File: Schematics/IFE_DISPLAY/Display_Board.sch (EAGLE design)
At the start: 48 parts, among them IC1 EP2C5T144, Q1 16MHz, U1 EPCS1SI8N, U2 MX150_8_PIN, U3 ATMEGA328P-AU, U4 HEX_CONVERTER, U5 HEX_CONVERTER, U6 MC7805BDD, U7 MCP1826S-1802E/DB, X3 16MHz

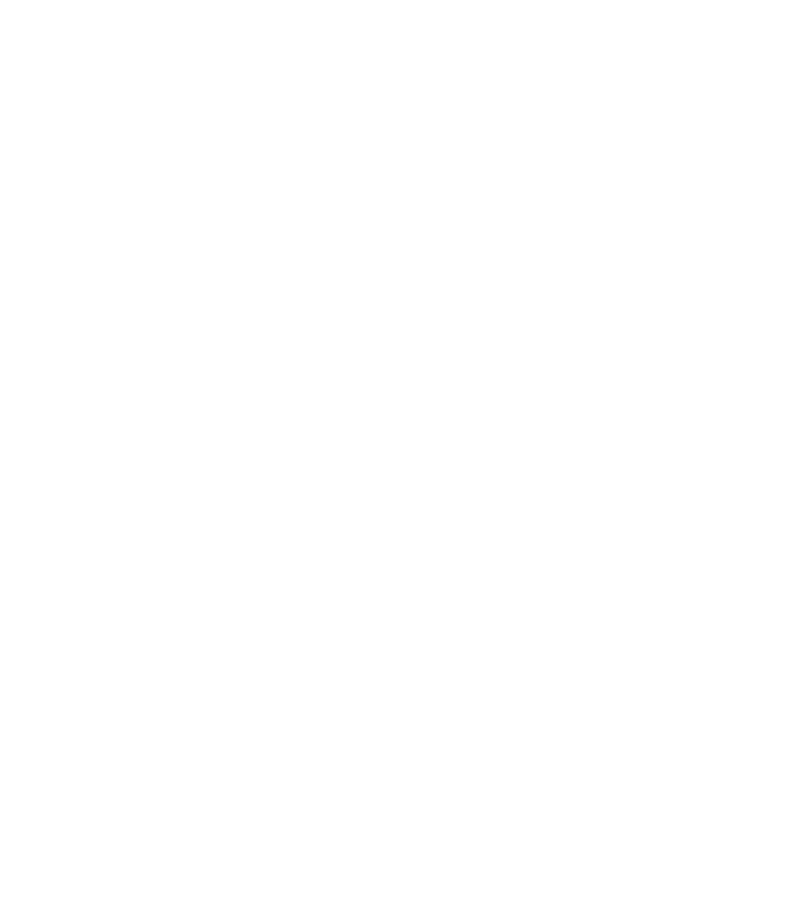
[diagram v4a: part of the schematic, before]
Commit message: Working on Breakout Board Layout
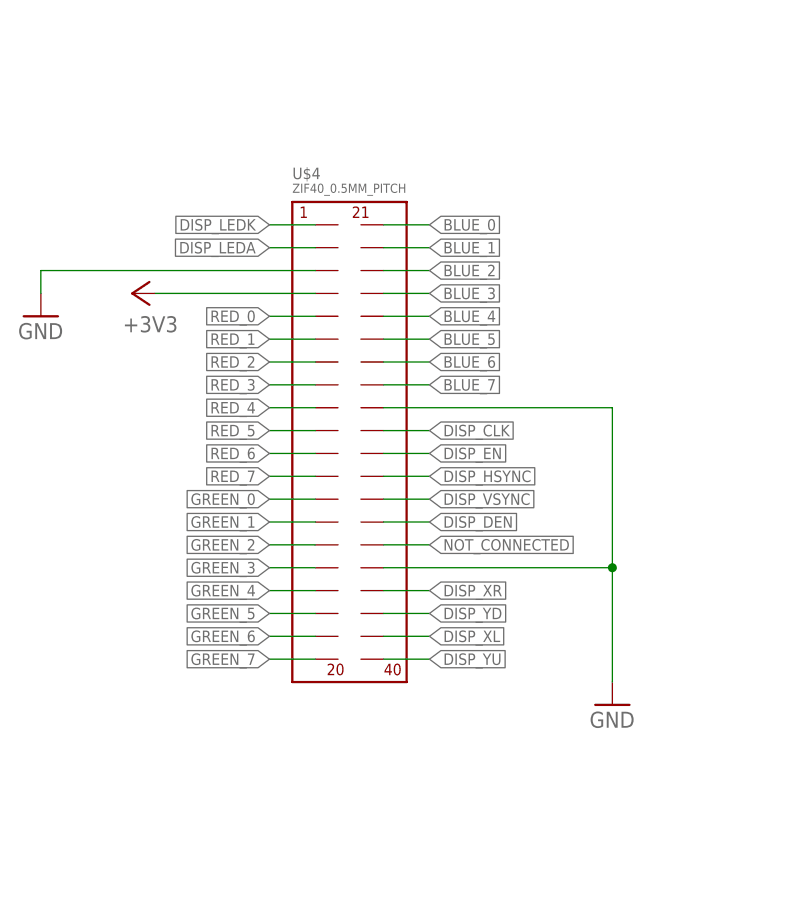
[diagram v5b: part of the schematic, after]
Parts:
- added U$4: ZIF40_0.5MM_PITCH, Connectors:ZIF40_0.5MM_PITCH
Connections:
- new net DISP_CLK: U$4.P$30
- new net DISP_DEN: U$4.P$34
- new net DISP_EN: U$4.P$31
- new net DISP_HSYNC: U$4.P$32
- new net DISP_LEDA: U$4.P$2
- new net DISP_LEDK: U$4.P$1
- new net DISP_VSYNC: U$4.P$33
- new net DISP_XL: U$4.P$39
- new net DISP_XR: U$4.P$37
- new net DISP_YD: U$4.P$38
- new net DISP_YU: U$4.P$40
- new net GREEN_3: U$4.P$16
- new net NOT_CONNECTED: U$4.P$35
- net +3V3: now also U$4.P$4
- net BLUE_0: now also U$4.P$21
- net BLUE_1: now also U$4.P$22
- net BLUE_2: now also U$4.P$23
- net BLUE_3: now also U$4.P$24
- net BLUE_4: now also U$4.P$25
- net BLUE_5: now also U$4.P$26
- net BLUE_6: now also U$4.P$27
- net BLUE_7: now also U$4.P$28
- net GND: now also U$4.P$29, U$4.P$3, U$4.P$36
- net GREEN_0: now also U$4.P$13
- net GREEN_1: now also U$4.P$14
- net GREEN_2: now also U$4.P$15
- net GREEN_4: now also U$4.P$17
- net GREEN_5: now also U$4.P$18
- net GREEN_6: now also U$4.P$19
- net GREEN_7: now also U$4.P$20
- net RED_0: now also U$4.P$5
- net RED_1: now also U$4.P$6
- net RED_2: now also U$4.P$7
- net RED_3: now also U$4.P$8
- net RED_4: now also U$4.P$9
- net RED_5: now also U$4.P$10
- net RED_6: now also U$4.P$11
- net RED_7: now also U$4.P$12

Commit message: figuring out DC-DC converters
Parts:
- removed C10: 0.1u, rcl:C-EUC0805K
- removed U$1: LM3940, Texas Instruments_By_element14_Batch_1:LM3940
- added D2: (no value), adafruit:DIODESMA
- added FUSE1: MINI297-3568, Fuse:MINI297-3568
- added R11, R16: 10k, rcl:R-US_R0805
- added U8: TPS5420D, Texas Instruments_By_element14_Batch_1:TPS5420D
- C1: value 0.1u -> 4.7uF; device rcl:C-EUC0805K -> resistor:C-EUC0805K
- C2: value 0.22u -> 0.01uF; device rcl:C-EUC0805K -> resistor:C-EUC0805K
- U6: value MC7805BDD -> TPS5420D; device IC's:MC7805BDD -> Texas Instruments_By_element14_Batch_1:TPS5420D
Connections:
- new net N$10: C2.2, U6.PH
- new net N$11: U6.VSENSE
- new net N$12: R11.1, R16.2, U6.ENA
- new net N$8: FUSE1.1, L2.1
- new net N$9: C2.1, U6.BOOT
- net +12V: now also C1.1, R11.2, U6.VIN; no longer C2.1, U6.IN
- net +3V3: no longer C10.1, U$1.VO, U7.VIN
- net +5V: no longer C1.1, U$1.VI, U6.OUT
- net GND: now also R16.1; no longer C10.2, C2.2, U$1.GND
- net PWR_IN: now also FUSE1.2; no longer L2.1
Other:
- moved on the sheet: C1, C11, C2, C5, L2, U7

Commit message: DCDC added need to adjust values
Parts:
- removed WIFI_: (no value), Headers_IFE:PINHD-2X4
- added C10, C12, C18, C19: 47uF, rcl:C-EUC0805K
- added C13, C20: 1800pF, rcl:C-EUC0805K
- added C14, C21: 0.1uF, rcl:C-EUC0805K
- added C15, C22: 150pF, rcl:C-EUC0805K
- added C16: 4.7uF, resistor:C-EUC0805K
- added C17: 0.01uF, resistor:C-EUC0805K
- added C23: 220u, Capacitors:C1206
- added D3: (no value), adafruit:DIODESMA
- added FUSE2: MINI297-3568, Fuse:MINI297-3568
- added L1: 23uH, Inductors:MSS7348
- added L3: 58uH, Inductors:MSS7348
- added L4: 20uH, Inductors:MSS7348
- added R17, R20, R21, R22: 10k, rcl:R-US_R0805
- added R18, R23: 5.9k, rcl:R-US_R0805
- added R19, R24: 549, rcl:R-US_R0805
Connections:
- net PWR_IN renamed PWR_IN_12
- new net +24V: C23.1, L4.2
- new net DISP_PWM: U3.PB1
- new net N$14: C14.2, R19.2
- new net N$15: C13.2, C14.1, C15.1, R17.1, R18.2, U6.VSENSE
- new net N$16: C17.1, U8.BOOT
- new net N$17: C17.2, D3.C, L3.1, U8.PH
- new net N$18: R20.1, R21.2, U8.ENA
- new net N$19: C20.2, C21.1, C22.1, R22.1, R23.2, U8.VSENSE
- new net N$20: C21.2, R24.2
- new net PWR_IN_24: FUSE2.2
- net +12V: now also C16.1, R20.2, U8.VIN
- net +3V3: now also C10.1, C12.1, C13.1, L1.2, R17.2, U7.VIN; no longer WIFI_.3, WIFI_.5, WIFI_.7
- net +5V: now also C18.1, C19.1, C20.1, L3.2, R22.2
- net GND: now also C10.2, C12.2, C15.2, C16.2, C18.2, C19.2, C22.2, C23.2, D2.A, D3.A, R18.1, R19.1, R21.1, R23.1, R24.1, U8.GND; no longer WIFI_.2
- net LED1: now also IC1.IO129
- net LED2: now also IC1.IO132
- net N$10: now also D2.C, L1.1
- net N$11: now also FUSE2.1, L4.1; no longer U6.VSENSE
- net RXD: no longer WIFI_.1
- net TXD_3_3: no longer WIFI_.8
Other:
- moved on the sheet: C1, C11, C2, C5, D2, FUSE1, L2, R11, R16, U6, U7, U8

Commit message: Finalizing Display Schematic
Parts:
- removed AS, JTAG: (no value), pinhead:PINHD-2X5
- removed C1, C16: 4.7uF, resistor:C-EUC0805K
- removed C10, C12, C18, C19: 47uF, rcl:C-EUC0805K
- removed C11: 0.1u, rcl:C-EUC0805K
- removed C13, C20: 1800pF, rcl:C-EUC0805K
- removed C14, C21: 0.1uF, rcl:C-EUC0805K
- removed C15, C22: 150pF, rcl:C-EUC0805K
- removed C17, C2: 0.01uF, resistor:C-EUC0805K
- removed C23, C5: 220u, Capacitors:C1206
- removed D2, D3: (no value), adafruit:DIODESMA
- removed FUSE1, FUSE2: MINI297-3568, Fuse:MINI297-3568
- removed IC1: EP2C5T144, altera-cyclone-II:EP2C5T144
- removed L1: 23uH, Inductors:MSS7348
- removed L2, L4: 20uH, Inductors:MSS7348
- removed L3: 58uH, Inductors:MSS7348
- removed QG1: SM77H, crystal:SM77H
- removed R1, R15, R2: 1K, resistor:R-US_R0805
- removed R11, R16, R17, R20, R21, R22: 10k, rcl:R-US_R0805
- removed R14: 10K, resistor:R-US_R0805
- removed R18, R23: 5.9k, rcl:R-US_R0805
- removed R19, R24: 549, rcl:R-US_R0805
- removed U6, U8: TPS5420D, Texas Instruments_By_element14_Batch_1:TPS5420D
- removed U7: MCP1826S-1802E/DB, Microchip_By_element14_Batch_1:MCP1826S-1802E/DB
- added AS1, JTAG1: (no value), pinhead:PINHD-2X5
- added C24, C40: 220u, Capacitors:C1206
- added C25: 0.1u, rcl:C-EUC0805K
- added C26, C33: 4.7uF, resistor:C-EUC0805K
- added C27, C34: 0.01uF, resistor:C-EUC0805K
- added C28, C29, C35, C36: 47uF, rcl:C-EUC0805K
- added C30, C37: 1800pF, rcl:C-EUC0805K
- added C31, C38: 0.1uF, rcl:C-EUC0805K
- added C32, C39: 150pF, rcl:C-EUC0805K
- added D4, D5: (no value), adafruit:DIODESMA
- added FUSE3, FUSE4: MINI297-3568, Fuse:MINI297-3568
- added IC2: EP2C5T144, altera-cyclone-II:EP2C5T144
- added L5, L8: 20uH, Inductors:MSS7348
- added L6: 23uH, Inductors:MSS7348
- added L7: 58uH, Inductors:MSS7348
- added Q2: MMBT3904L, transistor-npn:BCW31SMD
- added QG2: SM77H, crystal:SM77H
- added R25: 76, resistor:R-US_R0805
- added R26: 5.2k, resistor:R-US_R0805
- added R27, R28, R33: 1K, resistor:R-US_R0805
- added R29, R30, R31, R32: 10K, resistor:R-US_R0805
- added R34: 10k, rcl:R-US_R0805
- added R35: 5.9k, rcl:R-US_R0805
- added R36: 549, rcl:R-US_R0805
- added U$1: 776280-1, IFE_AMPSEAL_Conn:776280-1
- added U10, U9: TPS5420D, Texas Instruments_By_element14_Batch_1:TPS5420D
- R12: value 10K -> 5.9k; device resistor:R-US_R0805 -> rcl:R-US_R0805
- R13: value 10K -> 549; device resistor:R-US_R0805 -> rcl:R-US_R0805
- R3: value 10K -> 10k; device resistor:R-US_R0805 -> rcl:R-US_R0805
- U1: value EPCS1SI8N -> MCP1826S-1802E/DB; device Altera_By_element14_Batch_1:EPCS1SI8N -> Microchip_By_element14_Batch_1:MCP1826S-1802E/DB
- U2: value MX150_8_PIN -> EPCS1SI8N; device Connectors:MX150_8_PIN -> Altera_By_element14_Batch_1:EPCS1SI8N
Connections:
- removed net N$10: C2.2, D2.C, L1.1, U6.PH
- removed net N$11: FUSE2.1, L4.1
- removed net N$12: R11.1, R16.2, U6.ENA
- removed net N$14: C14.2, R19.2
- removed net N$15: C13.2, C14.1, C15.1, R17.1, R18.2, U6.VSENSE
- removed net N$16: C17.1, U8.BOOT
- removed net N$17: C17.2, D3.C, L3.1, U8.PH
- removed net N$18: R20.1, R21.2, U8.ENA
- removed net N$19: C20.2, C21.1, C22.1, R22.1, R23.2, U8.VSENSE
- removed net N$20: C21.2, R24.2
- removed net N$8: FUSE1.1, L2.1
- removed net N$9: C2.1, U6.BOOT
- removed net TXD_3_3: U5.6Y
- new net N$13: Q2.B, R26.1
- new net N$21: IC2.NSTATUS, R29.1
- new net N$22: C27.1, U9.BOOT
- new net N$23: C27.2, D4.C, L6.1, U9.PH
- new net N$25: C30.2, C31.1, C32.1, R12.2, R3.1, U9.VSENSE
- new net N$26: C31.2, R13.2
- new net N$27: C34.1, U10.BOOT
- new net N$28: C34.2, D5.C, L7.1, U10.PH
- new net N$30: C37.2, C38.1, C39.1, R34.1, R35.2, U10.VSENSE
- new net N$31: C38.2, R36.2
- new net N$32: FUSE4.1, L8.1
- net +12V: now also C24.1, C26.1, C33.1, L5.2, U10.ENA, U10.VIN, U9.ENA, U9.VIN; no longer C1.1, C16.1, C5.1, L2.2, R11.2, R20.2, U6.VIN, U8.VIN
- net +24V: now also C40.1, L8.2, R25.2; no longer C23.1, L4.2
- net +3V3: now also AS1.4, C28.1, C29.1, C30.1, IC2.VCC@1, IC2.VCC@10, IC2.VCC@11, IC2.VCC@12, IC2.VCC@13, IC2.VCC@16, IC2.VCC@18, IC2.VCC@2, IC2.VCC@20, IC2.VCC@3, IC2.VCC@6, IC2.VCC@8, JTAG1.4, L6.2, QG2.VCC, R28.1, R29.2, R31.2, R32.2, R33.2, U1.VIN, U2.VCC, U2.VCC_2, U2.VCC_3; no longer AS.4, C10.1, C12.1, C13.1, IC1.VCC@1, IC1.VCC@10, IC1.VCC@11, IC1.VCC@12, IC1.VCC@13, IC1.VCC@16, IC1.VCC@18, IC1.VCC@2, IC1.VCC@20, IC1.VCC@3, IC1.VCC@6, IC1.VCC@8, JTAG.4, L1.2, QG1.VCC, R13.2, R14.2, R15.2, R17.2, R2.1, R7.2, U1.VCC, U1.VCC_2, U1.VCC_3, U3.AVCC, U3.VCC, U3.VCC_2, U7.VIN
- net +5V: now also C35.1, C36.1, C37.1, L7.2, R34.2, R7.2, U3.AVCC, U3.VCC, U3.VCC_2; no longer C18.1, C19.1, C20.1, L3.2, R22.2
- net 50_MHZ: now also IC2.CLK0, QG2.OUT; no longer IC1.CLK0, QG1.OUT
- net ASDO: now also AS1.9, IC2.IO1, U2.ASDI; no longer AS.9, IC1.IO1, U1.ASDI
- net BLUE_0: now also IC2.IO52; no longer IC1.IO52
- net BLUE_1: now also IC2.IO53; no longer IC1.IO53
- net BLUE_2: now also IC2.IO55; no longer IC1.IO55
- net BLUE_3: now also IC2.IO57; no longer IC1.IO57
- net BLUE_4: now also IC2.IO58; no longer IC1.IO58
- net BLUE_5: now also IC2.IO59; no longer IC1.IO59
- net BLUE_6: now also IC2.IO60; no longer IC1.IO60
- net BLUE_7: now also IC2.IO63; no longer IC1.IO63
- net CANH: now also U$1.5; no longer U2.2
- net CANL: now also U$1.8; no longer U2.1
- net CONF_DONE: now also AS1.3, IC2.CONF_DONE, R32.1; no longer AS.3, IC1.CONF_DONE, R14.1
- net DATA0: now also AS1.7, IC2.DATA0, U2.DATA; no longer AS.7, IC1.DATA0, U1.DATA
- net DCLK: now also AS1.1, IC2.DCLK, U2.DCLK; no longer AS.1, IC1.DCLK, U1.DCLK
- net DISP_CLK: now also IC2.IO3
- net DISP_DEN: now also IC2.IO9
- net DISP_EN: now also IC2.IO4
- net DISP_HSYNC: now also IC2.IO7
- net DISP_LEDA: now also R25.1
- net DISP_LEDK: now also Q2.C
- net DISP_PWM: now also R26.2
- net DISP_VSYNC: now also IC2.IO8
- net FPGA_D0_3_3: now also IC2.IO142; no longer IC1.IO142
- net FPGA_D1_3_3: now also IC2.IO141; no longer IC1.IO141
- net FPGA_D2_3_3: now also IC2.IO139; no longer IC1.IO139
- net FPGA_D3_3_3: now also IC2.IO137; no longer IC1.IO137
- net FPGA_R0_3_3: now also IC2.IO136; no longer IC1.IO136
- net FPGA_R1_3_3: now also IC2.IO135; no longer IC1.IO135
- net FPGA_R2_3_3: now also IC2.IO134; no longer IC1.IO134
- net FPGA_R3_3_3: now also IC2.IO133; no longer IC1.IO133
- net FPGA_RSEL_3_3: now also IC2.IO144; no longer IC1.IO144
- net FPGA_W_3_3: now also IC2.IO143; no longer IC1.IO143
- net GND: now also AS1.10, AS1.2, C24.2, C25.2, C26.2, C28.2, C29.2, C32.2, C33.2, C35.2, C36.2, C39.2, C40.2, D4.A, D5.A, IC2.GND@1, IC2.GND@10, IC2.GND@11, IC2.GND@12, IC2.GND@13, IC2.GND@14, IC2.GND@15, IC2.GND@16, IC2.GND@17, IC2.GND@18, IC2.GND@19, IC2.GND@2, IC2.GND@20, IC2.GND@21, IC2.GND@22, IC2.GND@23, IC2.GND@3, IC2.GND@4, IC2.GND@5, IC2.GND@6, IC2.GND@7, IC2.GND@8, IC2.GND@9, IC2.MSEL0, IC2.MSEL1, JTAG1.10, JTAG1.2, Q2.E, QG2.GND, R12.1, R13.1, R27.1, R30.2, R35.1, R36.1, U$1.4, U1.GND_(TAB), U1.GND_(TAB)_2, U10.GND, U2.GND, U9.GND; no longer AS.10, AS.2, C1.2, C10.2, C11.2, C12.2, C15.2, C16.2, C18.2, C19.2, C22.2, C23.2, C5.2, D2.A, D3.A, IC1.GND@1, IC1.GND@10, IC1.GND@11, IC1.GND@12, IC1.GND@13, IC1.GND@14, IC1.GND@15, IC1.GND@16, IC1.GND@17, IC1.GND@18, IC1.GND@19, IC1.GND@2, IC1.GND@20, IC1.GND@21, IC1.GND@22, IC1.GND@23, IC1.GND@3, IC1.GND@4, IC1.GND@5, IC1.GND@6, IC1.GND@7, IC1.GND@8, IC1.GND@9, IC1.MSEL0, IC1.MSEL1, JTAG.10, JTAG.2, QG1.GND, R1.1, R12.2, R16.1, R18.1, R19.1, R21.1, R23.1, R24.1, U1.GND, U2.4, U6.GND, U7.GND_(TAB), U7.GND_(TAB)_2, U8.GND
- net GREEN_0: now also IC2.IO41; no longer IC1.IO41
- net GREEN_1: now also IC2.IO42; no longer IC1.IO42
- net GREEN_2: now also IC2.IO43; no longer IC1.IO43
- net GREEN_4: now also IC2.IO44; no longer IC1.IO44
- net GREEN_5: now also IC2.IO45; no longer IC1.IO45
- net GREEN_6: now also IC2.IO47; no longer IC1.IO47
- net GREEN_7: now also IC2.IO48; no longer IC1.IO48
- net GREEN_8: now also IC2.IO51; no longer IC1.IO51
- net LED1: now also IC2.IO129; no longer IC1.IO129
- net LED2: now also IC2.IO132; no longer IC1.IO132
- net N$1: now also FUSE3.1, L5.1; no longer IC1.NSTATUS, R3.1
- net NCE: now also AS1.6, IC2.NCE, R30.1; no longer AS.6, IC1.NCE, R12.1
- net NCONFIG: now also AS1.5, IC2.NCONFIG, R31.1; no longer AS.5, IC1.NCONFIG, R13.1
- net NCSO: now also AS1.8, IC2.IO2, U2.NCS; no longer AS.8, IC1.IO2, U1.NCS
- net PWR_IN_12: now also FUSE3.2, U$1.7; no longer FUSE1.2, U2.3
- net PWR_IN_24: now also FUSE4.2, U$1.6; no longer FUSE2.2
- net RED_0: now also IC2.IO25; no longer IC1.IO25
- net RED_1: now also IC2.IO26; no longer IC1.IO26
- net RED_2: now also IC2.IO27; no longer IC1.IO27
- net RED_3: now also IC2.IO28; no longer IC1.IO28
- net RED_4: now also IC2.IO30; no longer IC1.IO30
- net RED_5: now also IC2.IO31; no longer IC1.IO31
- net RED_6: now also IC2.IO32; no longer IC1.IO32
- net RED_7: now also IC2.IO40; no longer IC1.IO40
- net TCK: now also IC2.TCK, JTAG1.1, R27.2; no longer IC1.TCK, JTAG.1, R1.2
- net TDI: now also IC2.TDI, JTAG1.9, R28.2; no longer IC1.TDI, JTAG.9, R2.2
- net TDO: now also IC2.TDO, JTAG1.3; no longer IC1.TDO, JTAG.3
- net TMS: now also IC2.TMS, JTAG1.5, R33.1; no longer IC1.TMS, JTAG.5, R15.1
- net TXD: no longer U5.6A
- net VCC: now also C25.1, IC2.VCC@14, IC2.VCC@15, IC2.VCC@17, IC2.VCC@19, IC2.VCC@4, IC2.VCC@5, IC2.VCC@7, IC2.VCC@9, U1.VOUT; no longer C11.1, IC1.VCC@14, IC1.VCC@15, IC1.VCC@17, IC1.VCC@19, IC1.VCC@4, IC1.VCC@5, IC1.VCC@7, IC1.VCC@9, U7.VOUT
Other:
- note added: "Connector"
- note added: "Display PWM Circuitry"
- note added: "Display_Connector"
- note added: "Indicators"
- note added: "Level Shift for FPGA Ctrl"
